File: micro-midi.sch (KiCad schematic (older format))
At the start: 13 parts, among them J1 AudioJack3, J2 Conn_01x04_Male, J3 AudioJack3, U1 74HC04, U2 6N137, U3 74AHC04

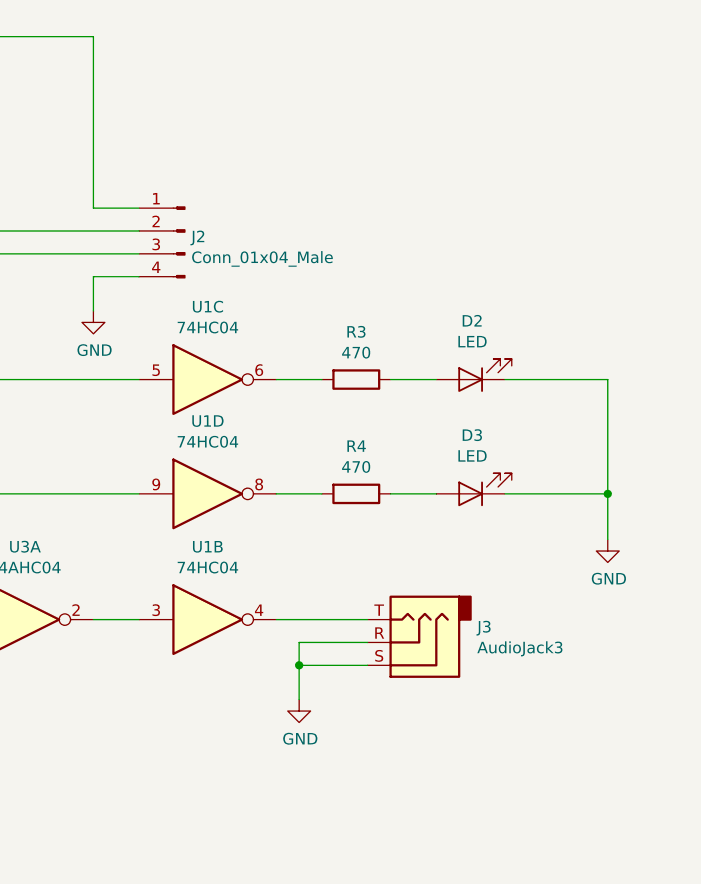
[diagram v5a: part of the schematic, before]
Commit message: fix midi out and add termination resistors
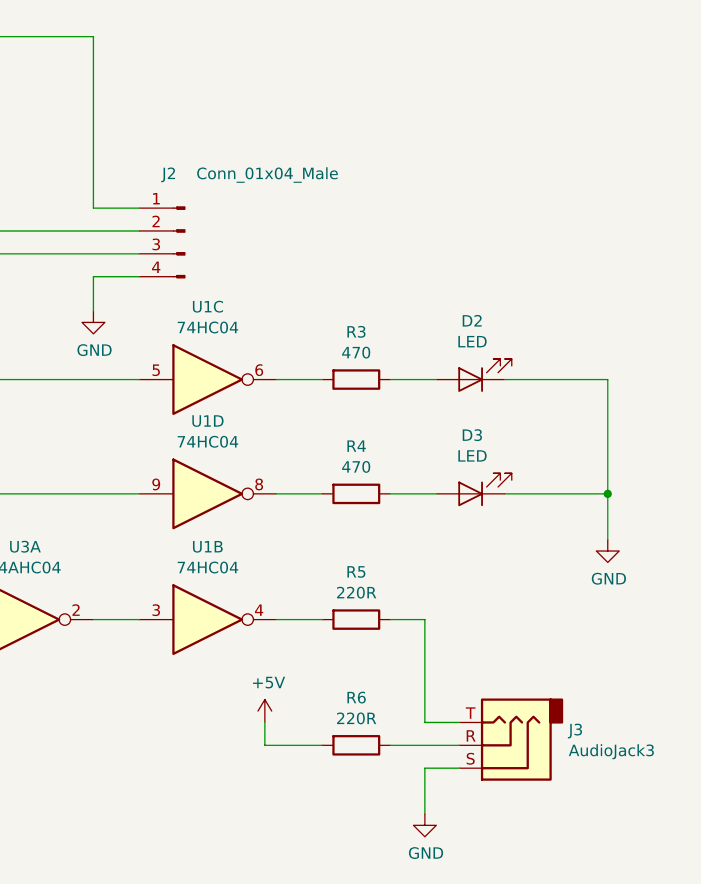
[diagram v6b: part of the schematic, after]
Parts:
- added R5, R6: 220R, Resistor_SMD:R_1206_3216Metric, symbol Device:R
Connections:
- net +5V: now also R6.2
- net GND: no longer J3.R
- net at U1.4: now also R5.2; no longer J3.T
- new net: J3.R, R6.1
- new net: J3.T, R5.1
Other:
- moved on the sheet: J3
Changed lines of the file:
@@
 U 1 1 5E8191AB
 P 7200 2800
-F 0 "J2" H 7172 2774 50  0000 R CNN
-F 1 "Conn_01x04_Male" H 7172 2683 50  0000 R CNN
+F 0 "J2" H 7300 3050 50  0000 R CNN
+F 1 "Conn_01x04_Male" H 7150 3050 50  0000 R CNN
 F 2 "" H 7200 2800 50  0001 C CNN
 F 3 "~" H 7200 2800 50  0001 C CNN
@@
 $EndComp
 $Comp
-L power:GND #PWR06
+L power:GND #PWR011
 U 1 1 5E8632E7
 P 9050 4150
-F 0 "#PWR06" H 9050 3900 50  0001 C CNN
+F 0 "#PWR011" H 9050 3900 50  0001 C CNN
 F 1 "GND" H 9055 3977 50  0000 C CNN
 F 2 "" H 9050 4150 50  0001 C CNN
@@
 	0    1    1    0
 $EndComp
-Wire Wire Line
-	7600 4500 8000 4500
 $Comp
 L Connector:AudioJack3 J3
 U 1 1 5E8296E3
-P 8200 4600
-F 0 "J3" H 7921 4533 50  0000 R CNN
-F 1 "AudioJack3" H 7921 4624 50  0000 R CNN
-F 2 "Connector_Audio:Jack_3.5mm_QingPu_WQP-PJ398SM_Vertical_CircularHoles" H 8200 4600 50  0001 C CNN
-F 3 "~" H 8200 4600 50  0001 C CNN
-	1    8200 4600
+P 8600 5050
+F 0 "J3" H 8321 4983 50  0000 R CNN
+F 1 "AudioJack3" H 8321 5074 50  0000 R CNN
+F 2 "Connector_Audio:Jack_3.5mm_QingPu_WQP-PJ398SM_Vertical_CircularHoles" H 8600 5050 50  0001 C CNN
+F 3 "~" H 8600 5050 50  0001 C CNN
+	1    8600 5050
 	-1   0    0    1
 $EndComp
-Wire Wire Line
-	7700 4600 7700 4700
-Wire Wire Line
-	8000 4600 7700 4600
-$Comp
-L power:GND #PWR05
+$Comp
+L power:GND #PWR06
 U 1 1 5E7D92E0
 P 5400 3150
-F 0 "#PWR05" H 5400 2900 50  0001 C CNN
+F 0 "#PWR06" H 5400 2900 50  0001 C CNN
 F 1 "GND" H 5405 2977 50  0000 C CNN
 F 2 "" H 5400 3150 50  0001 C CNN
@@
 $EndComp
 $Comp
-L power:PWR_FLAG #FLG0101
+L power:PWR_FLAG #FLG02
 U 1 1 5E9891C0
 P 4550 4550
-F 0 "#FLG0101" H 4550 4625 50  0001 C CNN
+F 0 "#FLG02" H 4550 4625 50  0001 C CNN
 F 1 "PWR_FLAG" H 4550 4723 50  0000 C CNN
 F 2 "" H 4550 4550 50  0001 C CNN
@@
 $EndComp
 $Comp
-L power:PWR_FLAG #FLG0102
+L power:PWR_FLAG #FLG01
 U 1 1 5E98E969
 P 4150 4900
-F 0 "#FLG0102" H 4150 4975 50  0001 C CNN
+F 0 "#FLG01" H 4150 4975 50  0001 C CNN
 F 1 "PWR_FLAG" H 4150 5073 50  0000 C CNN
 F 2 "" H 4150 4900 50  0001 C CNN
@@
 $EndComp
 $Comp
-L power:+5V #PWR04
+L power:+5V #PWR07
 U 1 1 5E7D8E69
 P 5600 1150
-F 0 "#PWR04" H 5600 1000 50  0001 C CNN
+F 0 "#PWR07" H 5600 1000 50  0001 C CNN
 F 1 "+5V" H 5615 1323 50  0000 C CNN
 F 2 "" H 5600 1150 50  0001 C CNN
@@
 $EndComp
 $Comp
-L power:+5V #PWR0101
+L power:+5V #PWR04
 U 1 1 5EA29925
 P 4150 4550
-F 0 "#PWR0101" H 4150 4400 50  0001 C CNN
+F 0 "#PWR04" H 4150 4400 50  0001 C CNN
 F 1 "+5V" H 4165 4723 50  0000 C CNN
 F 2 "" H 4150 4550 50  0001 C CNN
@@
 $EndComp
 $Comp
-L power:GND #PWR0102
+L power:GND #PWR05
 U 1 1 5EA29FD7
 P 4550 4900
-F 0 "#PWR0102" H 4550 4650 50  0001 C CNN
+F 0 "#PWR05" H 4550 4650 50  0001 C CNN
 F 1 "GND" H 4555 4727 50  0000 C CNN
 F 2 "" H 4550 4900 50  0001 C CNN
@@
 Wire Wire Line
 	4150 4550 4150 4900
-Wire Wire Line
-	7700 4700 8000 4700
-$Comp
-L power:GND #PWR?
+$Comp
+L power:GND #PWR010
 U 1 1 5EA4A4EF
-P 7700 4850
-F 0 "#PWR?" H 7700 4600 50  0001 C CNN
-F 1 "GND" H 7705 4677 50  0000 C CNN
-F 2 "" H 7700 4850 50  0001 C CNN
-F 3 "" H 7700 4850 50  0001 C CNN
-	1    7700 4850
-	1    0    0    -1
-$EndComp
-Wire Wire Line
-	7700 4700 7700 4850
-Connection ~ 7700 4700
+P 8250 5350
+F 0 "#PWR010" H 8250 5100 50  0001 C CNN
+F 1 "GND" H 8255 5177 50  0000 C CNN
+F 2 "" H 8250 5350 50  0001 C CNN
+F 3 "" H 8250 5350 50  0001 C CNN
+	1    8250 5350
+	1    0    0    -1
+$EndComp
 Wire Wire Line
 	5400 3000 5400 3150
 $Comp
-L power:GND #PWR?
+L power:GND #PWR08
 U 1 1 5EA55A66
 P 6800 3150
-F 0 "#PWR?" H 6800 2900 50  0001 C CNN
+F 0 "#PWR08" H 6800 2900 50  0001 C CNN
 F 1 "GND" H 6805 2977 50  0000 C CNN
 F 2 "" H 6800 3150 50  0001 C CNN
@@
 Wire Wire Line
 	5600 2800 5600 3950
+Wire Wire Line
+	7600 4500 7800 4500
+$Comp
+L Device:R R5
+U 1 1 5EA652C0
+P 7950 4500
+F 0 "R5" V 7743 4500 50  0000 C CNN
+F 1 "220R" V 7834 4500 50  0000 C CNN
+F 2 "Resistor_SMD:R_1206_3216Metric" V 7880 4500 50  0001 C CNN
+F 3 "~" H 7950 4500 50  0001 C CNN
+	1    7950 4500
+	0    1    1    0
+$EndComp
+Wire Wire Line
+	8100 4500 8250 4500
+Wire Wire Line
+	8250 4500 8250 4950
+Wire Wire Line
+	8250 4950 8400 4950
+$Comp
+L Device:R R6
+U 1 1 5EA76B1A
+P 7950 5050
+F 0 "R6" V 7743 5050 50  0000 C CNN
+F 1 "220R" V 7834 5050 50  0000 C CNN
+F 2 "Resistor_SMD:R_1206_3216Metric" V 7880 5050 50  0001 C CNN
+F 3 "~" H 7950 5050 50  0001 C CNN
+	1    7950 5050
+	0    1    1    0
+$EndComp
+Wire Wire Line
+	8100 5050 8400 5050
+$Comp
+L power:+5V #PWR09
+U 1 1 5EA789B7
+P 7550 4950
+F 0 "#PWR09" H 7550 4800 50  0001 C CNN
+F 1 "+5V" H 7565 5123 50  0000 C CNN
+F 2 "" H 7550 4950 50  0001 C CNN
+F 3 "" H 7550 4950 50  0001 C CNN
+	1    7550 4950
+	1    0    0    -1
+$EndComp
+Wire Wire Line
+	7550 4950 7550 5050
+Wire Wire Line
+	7550 5050 7800 5050
+Wire Wire Line
+	8400 5150 8250 5150
+Wire Wire Line
+	8250 5150 8250 5350
 $EndSCHEMATC
